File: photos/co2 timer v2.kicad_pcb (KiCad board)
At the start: 2 copper layers, 65 x 45 mm, 27 parts, among them J1 9V_IN, J2 SOLENOID, J3 ICSP, J4 TM1637, Q1 IRL540NPBF, SW1 UP, SW2 SET, U1 ATtiny85-20PU, U2 DS3231SN, U3 AMS1117-3.3

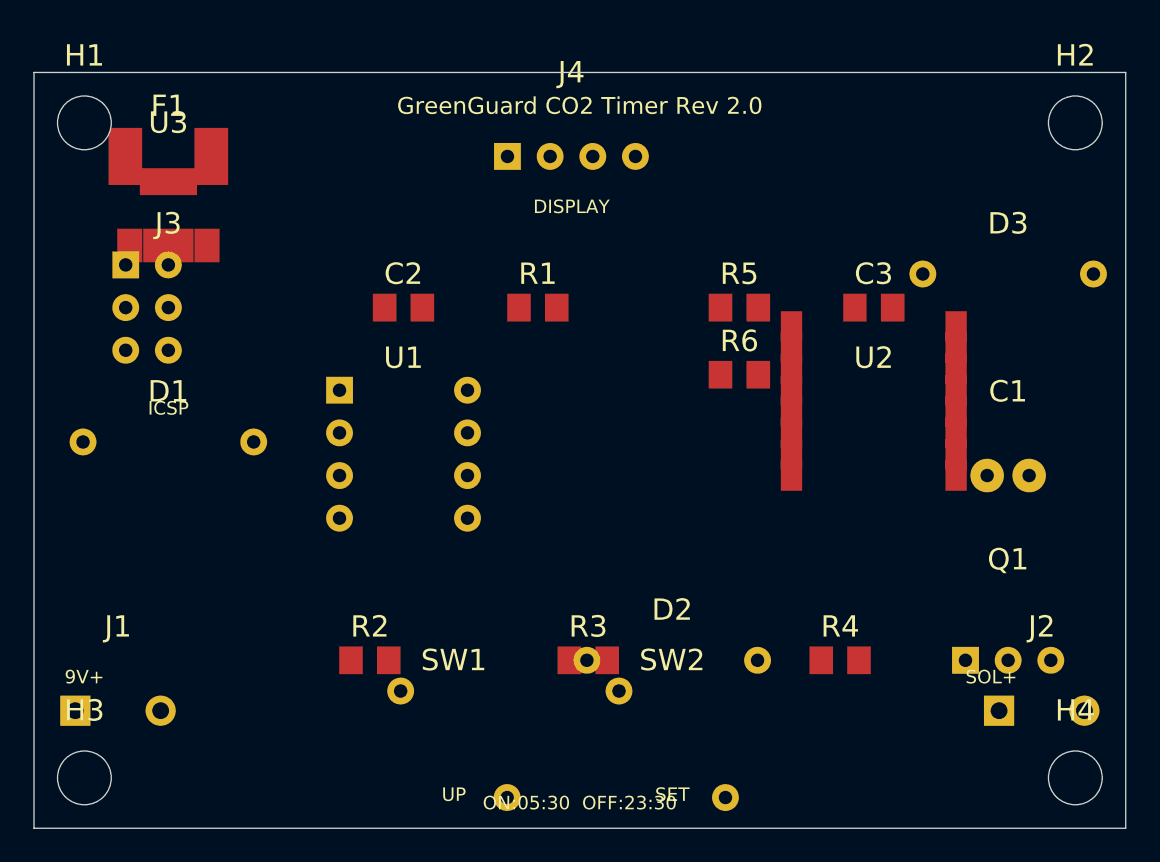
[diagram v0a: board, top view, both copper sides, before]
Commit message: Sync deployed GreenGuard web app state to git
Snapshot of deployed-but-uncommitted work that had accumulated in the
working tree (the reason fixes kept appearing 'lost' each session):
- 92 modified files (app/pages, app/lib, app/components, astro/src, etc.)
- 28 new deployed API endpoints (admin data routes, book/slots,
  cron/ads-tracking-health, gbp-post/reply, etc.) + design-sync styles
- remove dead app/lib/gnl.js

Excludes: build artifacts (app/dist, ds-bundle, design-sync), the
unrelated Cooling_Tower Ignition project files, and the other session's
astro/public prototype binaries.
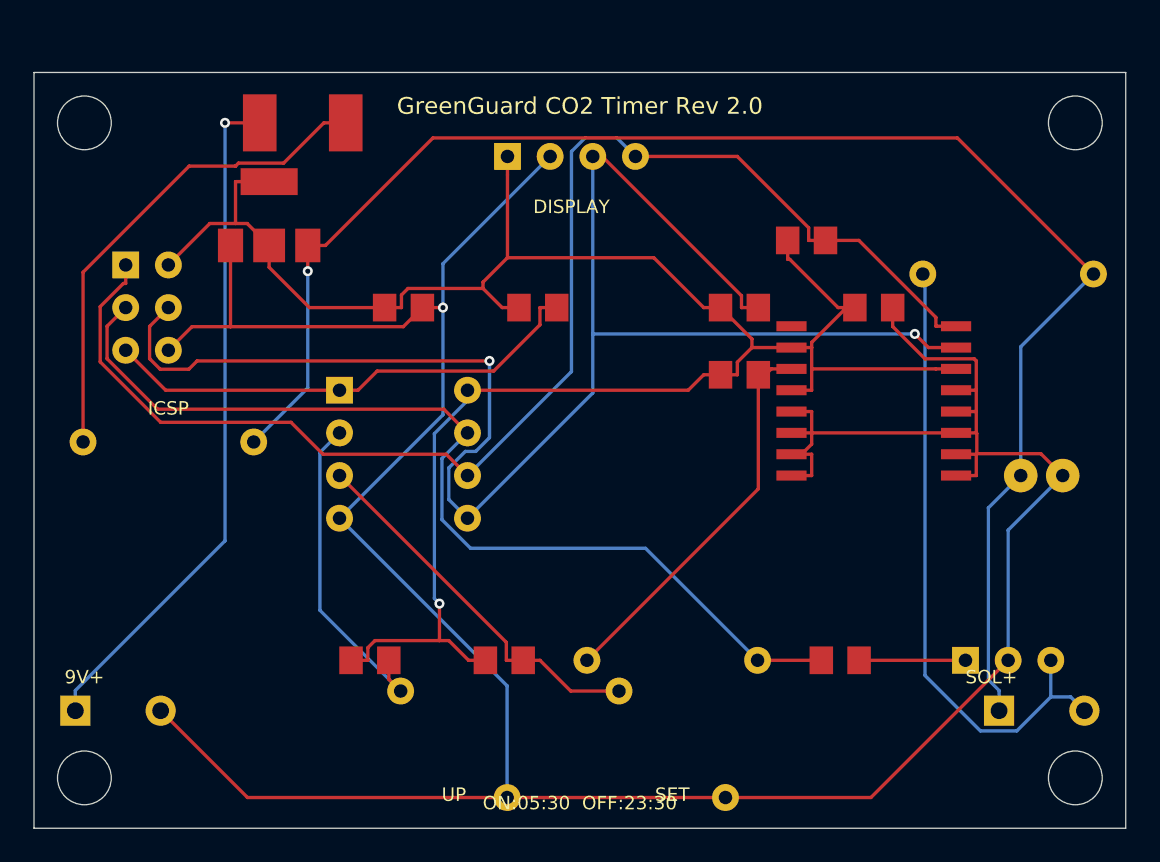
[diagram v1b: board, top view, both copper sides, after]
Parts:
- added R7: 4K7_SCL, Resistor_SMD:R_0805_2012Metric, F.Cu at (46.0, 10.0)
- moved F1 8.25 mm to (16.0, 3.00)
- moved U3 6.00 mm to (14.0, 8.00)
- moved R3 5.00 mm to (28.0, 35.0)
- moved C1 2.00 mm to (60.0, 24.0)
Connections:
- C1 pad +: (no net) -> +9V_RAW
- C1 pad -: (no net) -> GND
- C2 pad 1: (no net) -> +3V3
- C2 pad 2: (no net) -> GND
- C3 pad 1: (no net) -> +3V3
- C3 pad 2: (no net) -> GND
- D1 pad A: (no net) -> D1_ANODE
- D1 pad K: (no net) -> +9V_RAW
- D2 pad A: (no net) -> RTC_INT
- D2 pad K: (no net) -> PB2_CTRL
- D3 pad A: (no net) -> SOLENOID_DRAIN
- D3 pad K: (no net) -> +9V_RAW
- F1 pad 1: (no net) -> BATT_RAW
- F1 pad 2: (no net) -> D1_ANODE
- J1 pad 1: (no net) -> BATT_RAW
- J1 pad 2: (no net) -> GND
- J2 pad 1: (no net) -> +9V_RAW
- J2 pad 2: (no net) -> SOLENOID_DRAIN
- J3 pad 1: (no net) -> SCL_DIO
- J3 pad 2: (no net) -> +3V3
- J3 pad 3: (no net) -> PB2_CTRL
- J3 pad 4: (no net) -> SDA_CLK
- J3 pad 5: (no net) -> RESET_N
- J3 pad 6: (no net) -> GND
- J4 pad 1: (no net) -> +3V3
- J4 pad 2: (no net) -> GND
- J4 pad 3: (no net) -> SDA_CLK
- J4 pad 4: (no net) -> SCL_DIO
- Q1 pad 1: (no net) -> GATE_NET
- Q1 pad 2: (no net) -> GND
- Q1 pad 3: (no net) -> SOLENOID_DRAIN
- R1 pad 1: (no net) -> +3V3
- R1 pad 2: (no net) -> RESET_N
- R2 pad 1: (no net) -> +3V3
- R2 pad 2: (no net) -> BTN_UP
- R3 pad 1: (no net) -> +3V3
- R3 pad 2: (no net) -> BTN_SET
- R4 pad 1: (no net) -> PB2_CTRL
- R4 pad 2: (no net) -> GATE_NET
- R5 pad 1: (no net) -> +3V3
- R5 pad 2: (no net) -> SDA_CLK
- R6 pad 1: (no net) -> +3V3
- R6 pad 2: (no net) -> RTC_INT
- SW1 pad 1: (no net) -> BTN_UP
- SW1 pad 2: (no net) -> GND
- SW2 pad 1: (no net) -> BTN_SET
- SW2 pad 2: (no net) -> GND
- U1 pad 1: (no net) -> RESET_N
- U1 pad 2: (no net) -> BTN_UP
- U1 pad 3: (no net) -> BTN_SET
- U1 pad 4: (no net) -> GND
- U1 pad 5: (no net) -> SDA_CLK
- U1 pad 6: (no net) -> SCL_DIO
- U1 pad 7: (no net) -> PB2_CTRL
- U1 pad 8: (no net) -> +3V3
- U2 pad 10: (no net) -> GND
- U2 pad 11: (no net) -> GND
- U2 pad 12: (no net) -> GND
- U2 pad 13: (no net) -> GND
- U2 pad 14: (no net) -> +3V3
- U2 pad 15: (no net) -> SDA_CLK
- U2 pad 16: (no net) -> SCL_DIO
- U2 pad 2: (no net) -> +3V3
- U2 pad 3: (no net) -> RTC_INT
- U2 pad 4: (no net) -> +3V3
- U2 pad 5: (no net) -> GND
- U2 pad 6: (no net) -> GND
- U2 pad 7: (no net) -> GND
- U2 pad 8: (no net) -> GND
- U2 pad 9: (no net) -> GND
- U3 pad 1: (no net) -> GND
- U3 pad 2: (no net) -> +3V3
- U3 pad 3: (no net) -> +9V_RAW
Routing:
- net GND: track 0.00 -> 181.0 mm, vias 0 -> 1
- net +3V3: track 0.00 -> 125.3 mm, vias 0 -> 1
- net SDA_CLK: track 0.00 -> 96.0 mm, vias 0 -> 2
- net +9V_RAW: track 0.00 -> 94.7 mm, vias 0 -> 1
- net SCL_DIO: track 0.00 -> 81.6 mm
- net PB2_CTRL: track 0.00 -> 58.6 mm
- net BATT_RAW: track 0.00 -> 40.8 mm, vias 0 -> 1
- net SOLENOID_DRAIN: track 0.00 -> 38.2 mm
- net D1_ANODE: track 0.00 -> 29.4 mm
- net RESET_N: track 0.00 -> 29.3 mm
- net RTC_INT: track 0.00 -> 23.3 mm
- net BTN_SET: track 0.00 -> 22.6 mm
- net BTN_UP: track 0.00 -> 20.0 mm
- net GATE_NET: track 0.00 -> 6.34 mm
